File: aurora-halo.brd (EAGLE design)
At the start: 60 x 42 mm, 9 parts

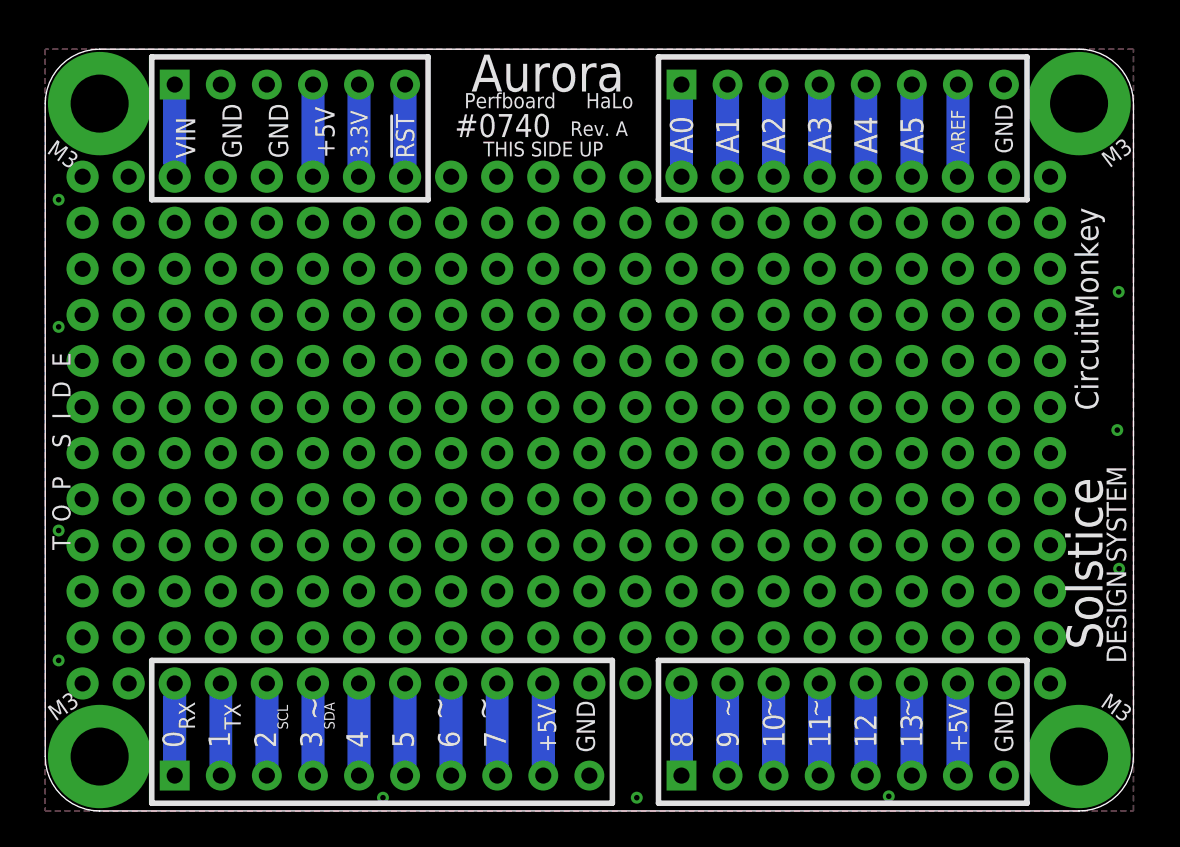
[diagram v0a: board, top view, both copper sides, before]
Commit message: Update PCB to Rev. B
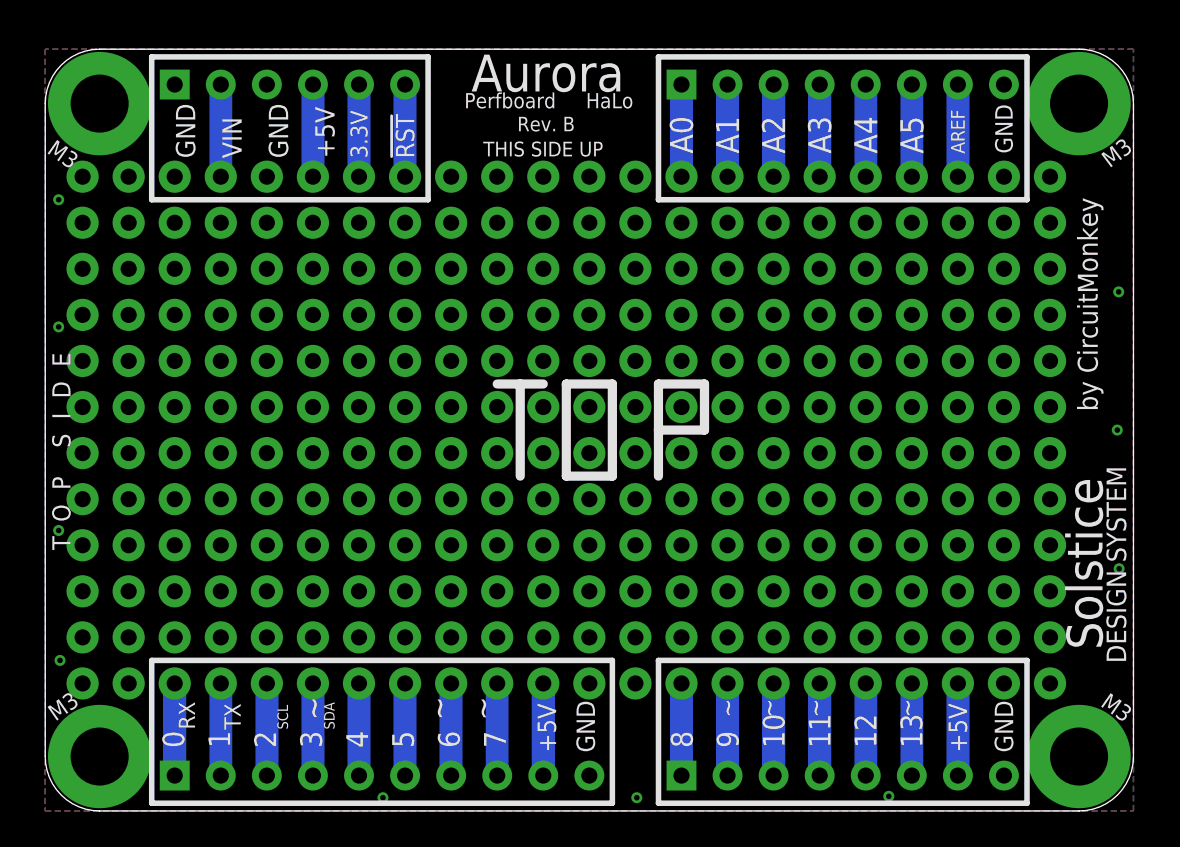
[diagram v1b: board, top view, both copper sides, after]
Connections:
- net GND: now also G4.3, HL4.1; no longer G4.4, HL4.2
- net VIN: now also G4.4, HL4.2; no longer G4.3, HL4.1
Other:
- board text added: "OPEN SOURCE"
- board text added: "Rev. B"
- board text added: "by CircuitMonkey"
- board text removed: "#0740"
- board text removed: "CircuitMonkey"
- board text removed: "Rev. A"
